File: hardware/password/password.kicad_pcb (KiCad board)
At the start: 2 copper layers, 100 x 100 mm, 62 parts, among them J1 RJ45_Shielded, SW1 SW_DIP_x01, SW10 SW_DIP_x01, SW11 SW_DIP_x01, SW2 SW_DIP_x01, SW3 SW_DIP_x01, SW4 SW_DIP_x01, SW5 SW_DIP_x01, SW6 SW_DIP_x01, SW7 SW_DIP_x01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

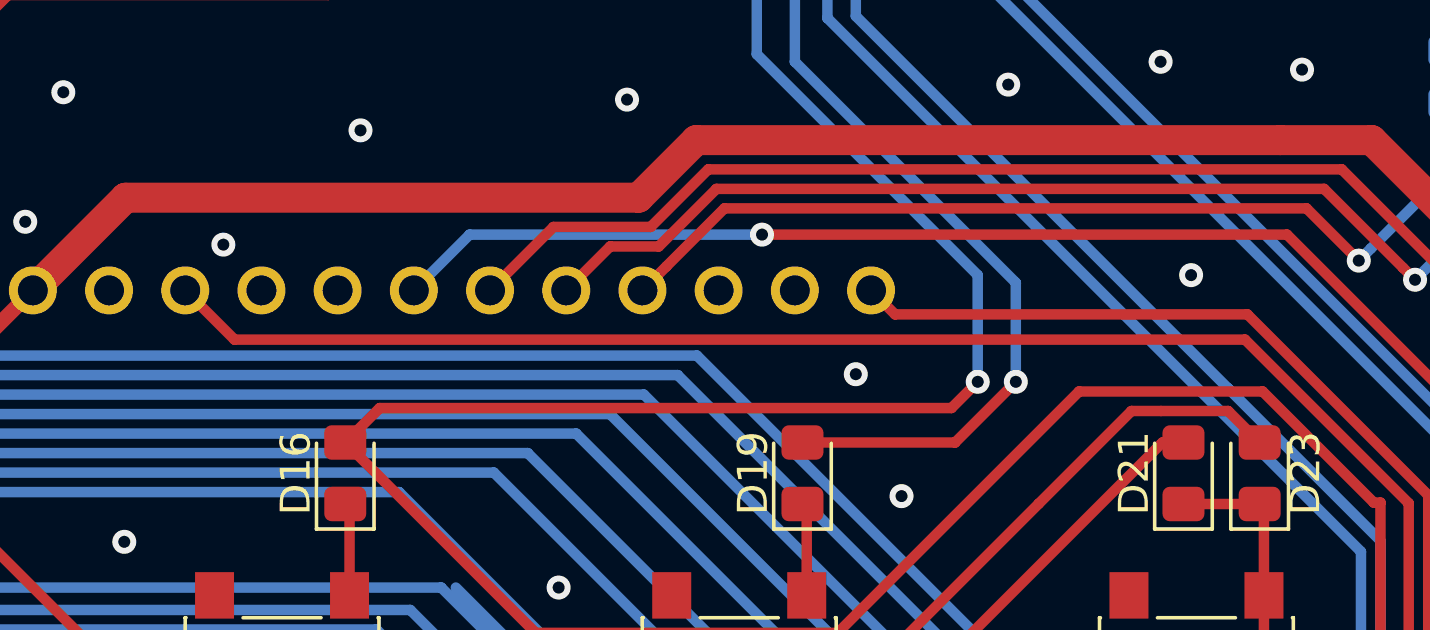
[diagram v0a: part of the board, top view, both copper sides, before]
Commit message: Password PCB: swap ADC-only pin A6 for A5
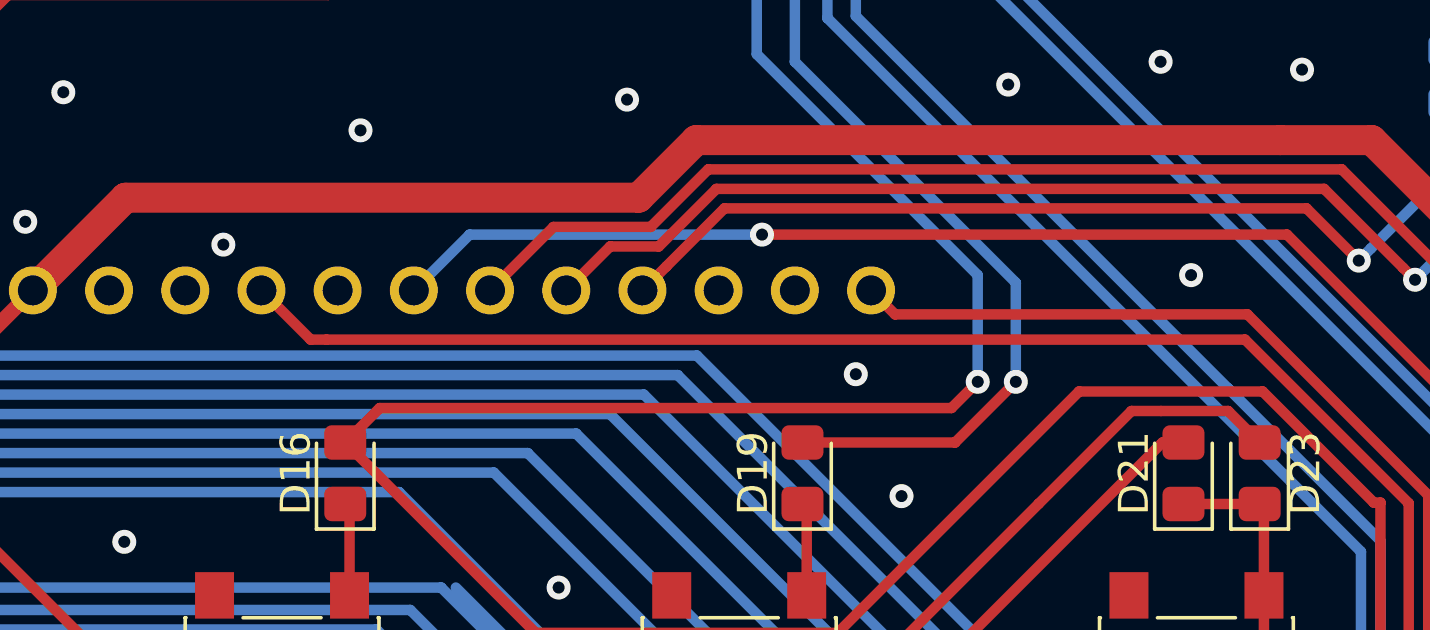
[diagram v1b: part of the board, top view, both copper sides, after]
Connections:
- SW11 pad 2: A6 -> A5_SCL
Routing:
- net A6: track 133.1 -> 0.00 mm
- net A5_SCL: track 0.00 -> 130.5 mm

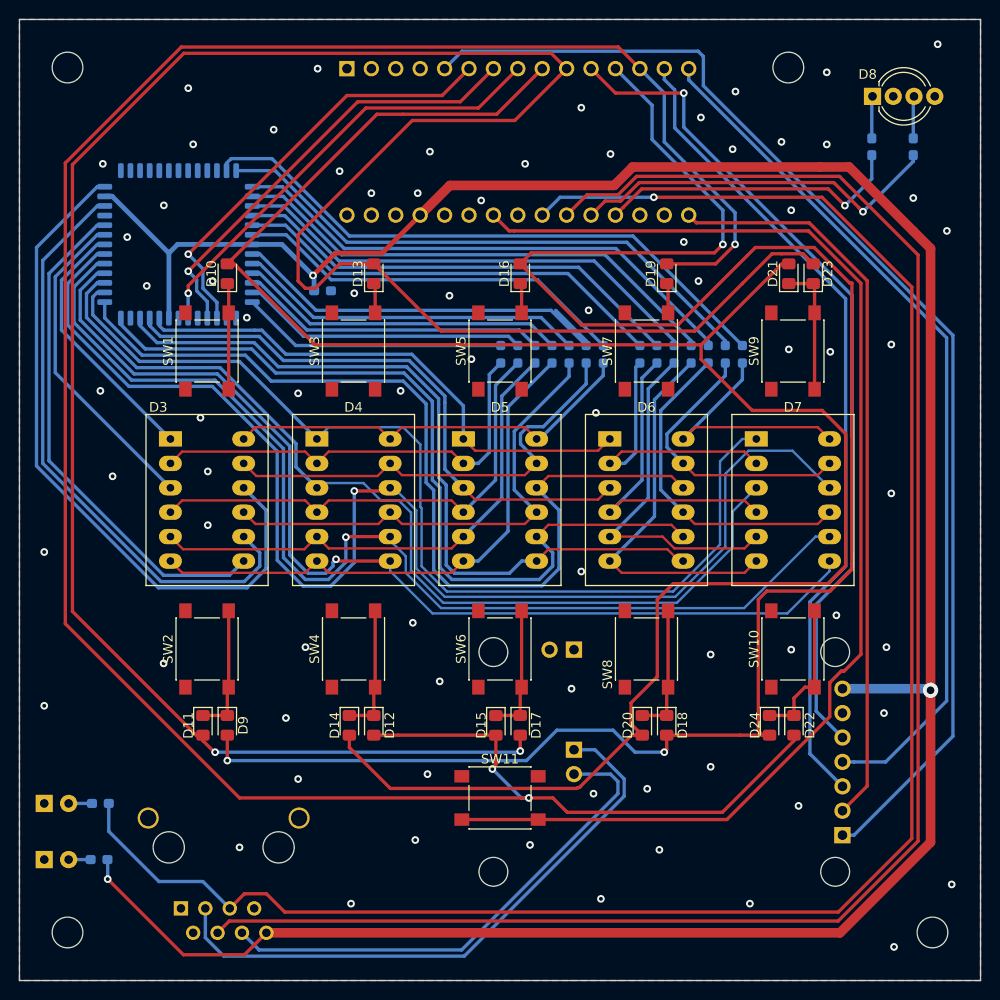
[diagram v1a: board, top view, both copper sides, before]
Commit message: Avoid using D10 (SPI SS) pin as input
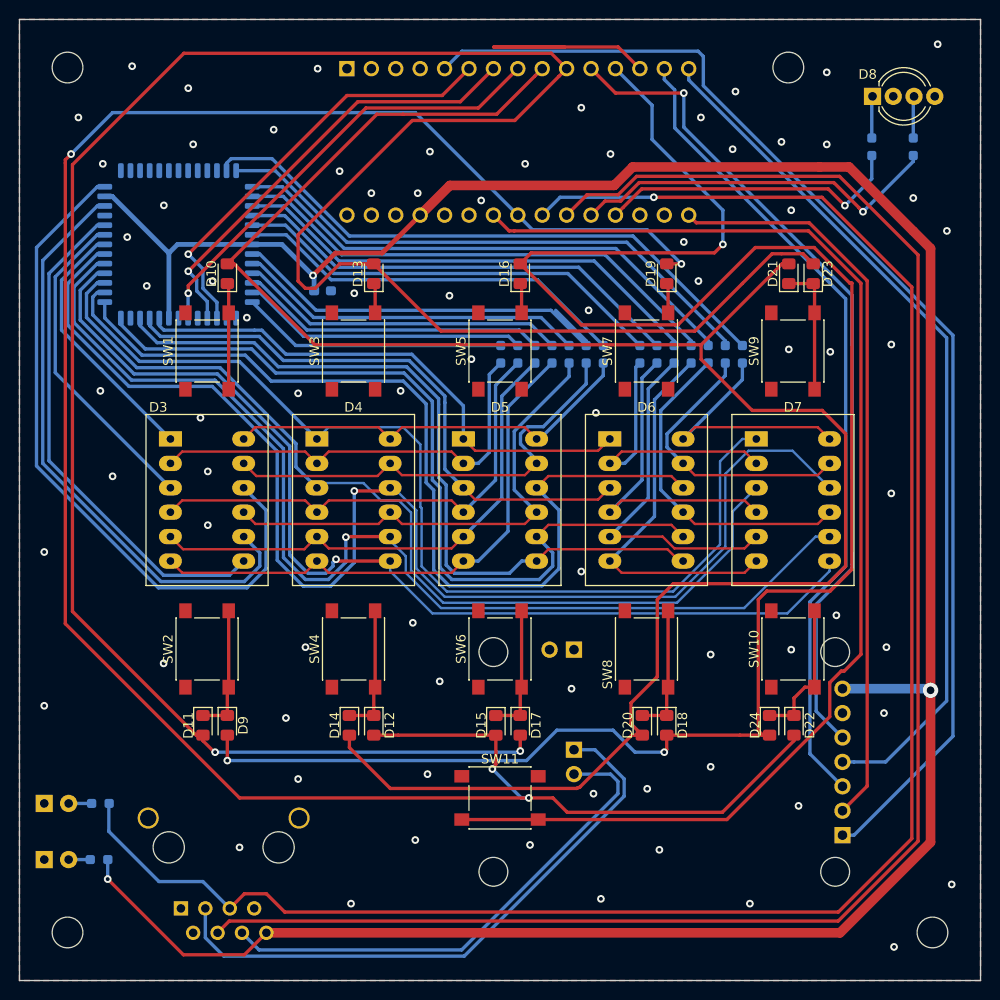
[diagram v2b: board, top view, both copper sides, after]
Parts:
- R1, R2, R28, R29: footprint Resistor_SMD:R_0603_1608Metric_Pad1.05x0.95mm_HandSolder -> Resistor_SMD:R_0603_1608Metric_Pad0.98x0.95mm_HandSolder
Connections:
- D12 pad 2: D10 -> A4_SDA
- D15 pad 2: D10 -> A4_SDA
- D19 pad 2: D10 -> A4_SDA
- D22 pad 2: D10 -> A4_SDA
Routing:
- net A4_SDA: track 0.00 -> 231.5 mm, vias 0 -> 4
- net D10: track 253.0 -> 23.5 mm, vias 3 -> 0
- net GND: vias 75 -> 77
